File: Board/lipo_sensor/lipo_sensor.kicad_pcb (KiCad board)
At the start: 2 copper layers, 33 x 30.5 mm, 27 parts, among them IC1 ATMEGA328P-A, P1 CONN_02X03, P2 CONN_01X03, P3 CONN_01X07, P4 CONN_01X03, X1 CRYSTAL_SMD, Y1 Crystal

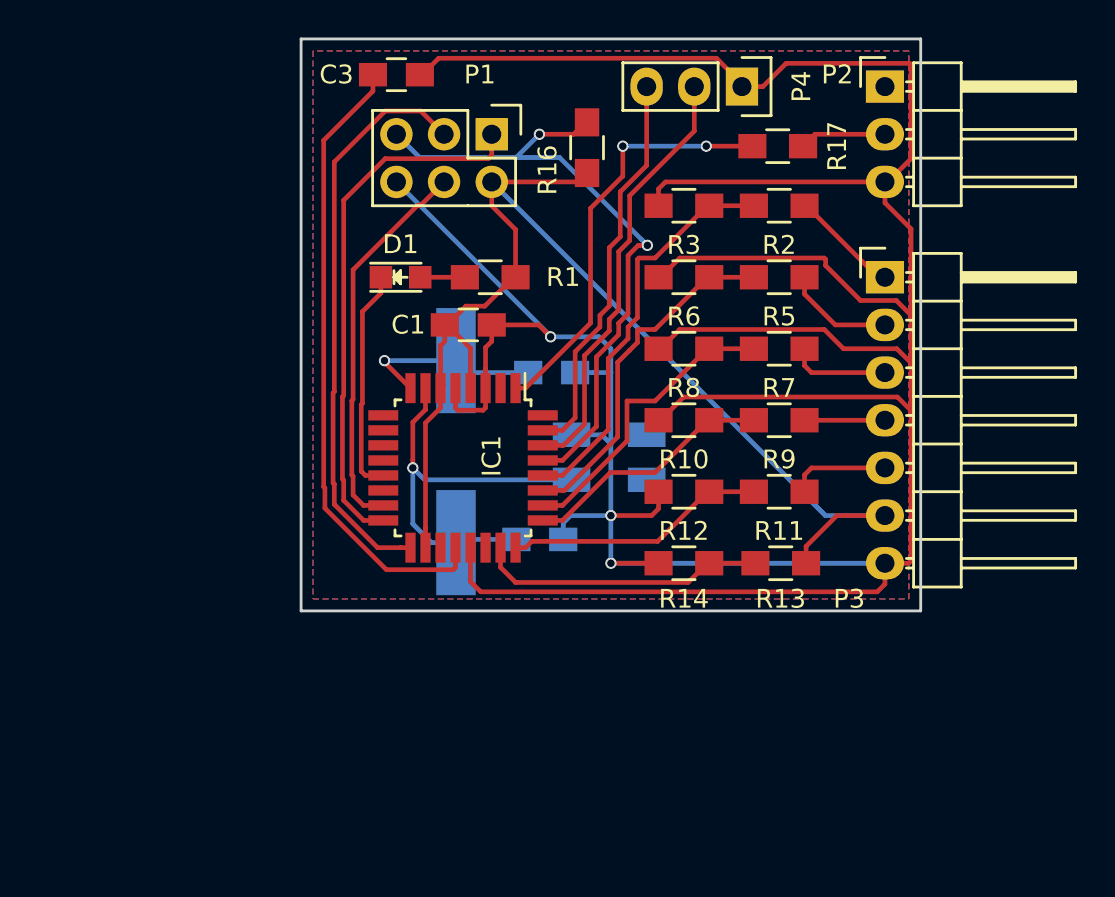
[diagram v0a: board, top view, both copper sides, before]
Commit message: Shrink layout and fix oszillator connections.
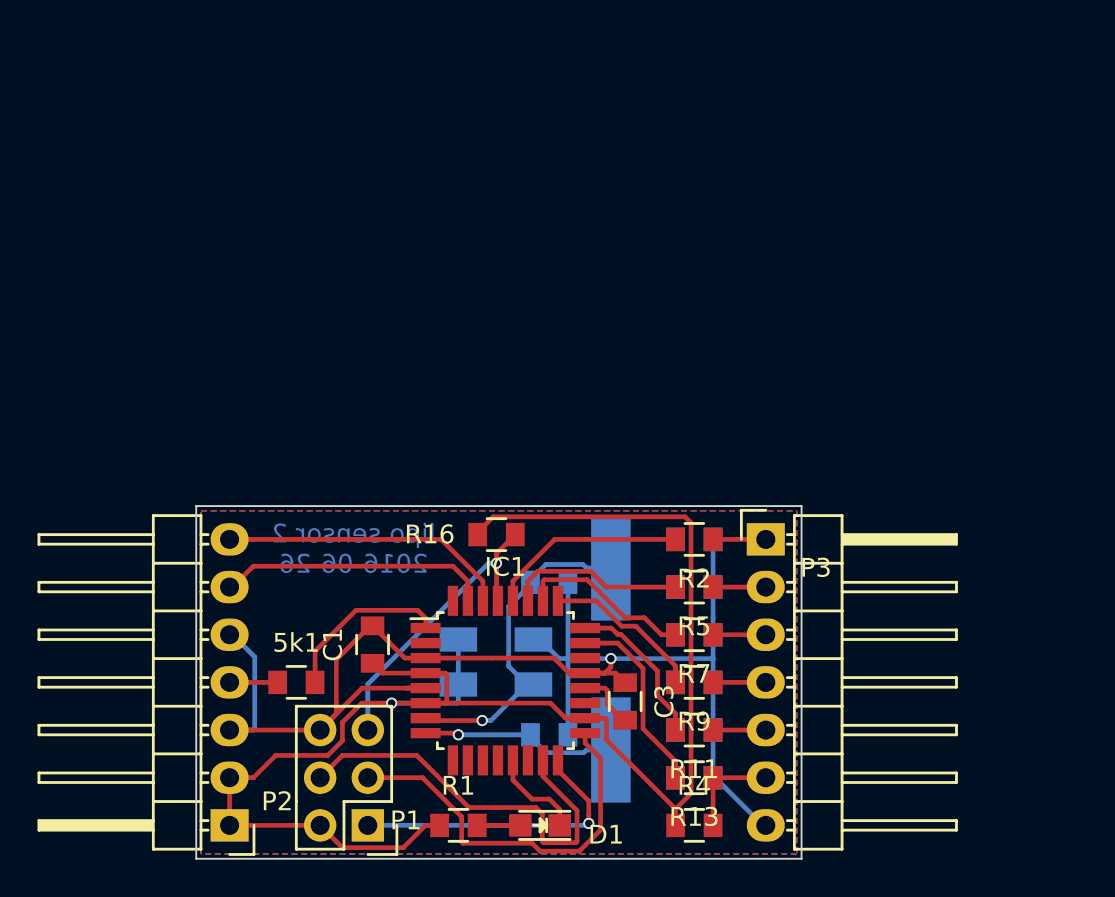
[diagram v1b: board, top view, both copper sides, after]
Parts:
- removed R17: 5k, Resistors_SMD:R_0805_HandSoldering
- removed X1: CRYSTAL_SMD, Crystals:Crystal_SMD_5032_4Pads
- added 5k1: 4k7, Capacitors_SMD:C_0805, F.Cu at (148.3, 110.5)
- added R4: 0, Capacitors_SMD:C_0805, F.Cu at (169.5, 118.1)
- C1, C3: footprint Capacitors_SMD:C_0805_HandSoldering -> Capacitors_SMD:C_0805
- C2, C5: value 16pF -> 22pF; footprint Capacitors_SMD:C_0805_HandSoldering -> Capacitors_SMD:C_0805
- P2: value CONN_01X03 -> CONN_01X07; footprint Pin_Headers:Pin_Header_Angled_1x03 -> Pin_Headers:Pin_Header_Angled_1x07
- P4: value CONN_01X03 -> OSZILLATOR; footprint Pin_Headers:Pin_Header_Straight_1x03 -> Cody_Footprints:Oszillator_SMD_5032_4Pads; moved to B.Cu
- R1: value 600 -> 680; footprint Resistors_SMD:R_0805_HandSoldering -> Capacitors_SMD:C_0805
- R10: value R -> 1k8; footprint Resistors_SMD:R_0805_HandSoldering -> Capacitors_SMD:C_0805; moved to B.Cu
- R11: value R -> 15k; footprint Resistors_SMD:R_0805_HandSoldering -> Capacitors_SMD:C_0805
- R12: value R -> 2k2; footprint Resistors_SMD:R_0805_HandSoldering -> Capacitors_SMD:C_0805; moved to B.Cu
- R13: value R -> 12k; footprint Resistors_SMD:R_0805_HandSoldering -> Capacitors_SMD:C_0805
- R14: value R -> 3k9; footprint Resistors_SMD:R_0805_HandSoldering -> Capacitors_SMD:C_0805; moved to B.Cu
- R16: footprint Resistors_SMD:R_0805_HandSoldering -> Capacitors_SMD:C_0805
- R2, R5, R9: value R -> 22k; footprint Resistors_SMD:R_0805_HandSoldering -> Capacitors_SMD:C_0805
- R3, R6: value R -> 1k; footprint Resistors_SMD:R_0805_HandSoldering -> Capacitors_SMD:C_0805; moved to B.Cu
- R7: value R -> 18k; footprint Resistors_SMD:R_0805_HandSoldering -> Capacitors_SMD:C_0805
- R8: value R -> 1k2; footprint Resistors_SMD:R_0805_HandSoldering -> Capacitors_SMD:C_0805; moved to B.Cu
- moved P2 52.6 mm to (144.8, 118.1), turned to 180 degrees
- moved P1 37.4 mm to (152.1, 118.1), turned to 180 degrees
- moved C3 35.6 mm to (165.9, 111.5), turned to 270 degrees
- moved P4 33.4 mm to (159.0, 109.4), turned to 0 degrees
- moved D1 30.1 mm to (161.3, 118.1), turned to 180 degrees
- moved R1 29.3 mm to (157.0, 118.1), turned to 0 degrees
- moved R16 21.2 mm to (159.0, 102.6), turned to 0 degrees
- moved C5 19.3 mm to (161.8, 113.3)
- moved R2 18.3 mm to (169.5, 102.9)
- moved R3 17.8 mm to (169.5, 102.9), turned to 0 degrees
- moved C1 17.8 mm to (152.4, 108.5), turned to 90 degrees
- moved R5 17.1 mm to (169.5, 105.4)
- moved R6 16.5 mm to (169.5, 105.4), turned to 0 degrees
- moved R7 15.9 mm to (169.5, 108.0)
- moved P3 15.3 mm to (173.4, 102.9)
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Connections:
- P2 pad 1: (no net) -> VCC
- P2 pad 2: Net-(P2-Pad2) -> VCC
- P3 pad 6: VCC -> Net-(P3-Pad6)
- P4 pad 1: GND -> VCC
- P4 pad 2: /RX -> GND
- P4 pad 3: /TX -> Net-(C2-Pad2)
- R13 pad 1: VCC -> Net-(P3-Pad6)
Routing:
- net GND: track 205.5 -> 77.6 mm, vias 3 -> 1
- net Net-(C3-Pad2): track 33.6 -> 3.28 mm
- net Net-(IC1-Pad29): track 35.1 -> 16.0 mm, vias 2 -> 1
- net VCC: track 68.9 -> 84.8 mm, vias 0 -> 1
- net /S.Port: track 22.5 -> 9.16 mm, vias 2 -> 0
- net Net-(IC1-Pad16): track 28.6 -> 15.9 mm, vias 0 -> 1
- net /Cell6: track 21.6 -> 10.6 mm
- net Net-(IC1-Pad17): track 30.8 -> 20.8 mm
- net /Cell5: track 18.6 -> 9.48 mm
- net /RX: track 23.6 -> 15.5 mm
- net /LED: track 12.0 -> 5.04 mm
- net /TX: track 21.2 -> 14.5 mm
- net /Cell4: track 16.0 -> 9.36 mm
- net /Cell2: track 13.9 -> 8.35 mm
- net Net-(P3-Pad6): track 0.00 -> 5.35 mm
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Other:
- board size 33 x 30.5 mm -> 32.3 x 18.8 mm
- net class Default: clearance 0.25 -> 0.2
- rule pad_to_mask_clearance: 0.2 -> 0
- rule trace_clearance: 0.25 -> 0.2
- board text added: "lipo sensor 2 2016-06-26"
- board text removed: "lipo sensor 1 2016-04-26"

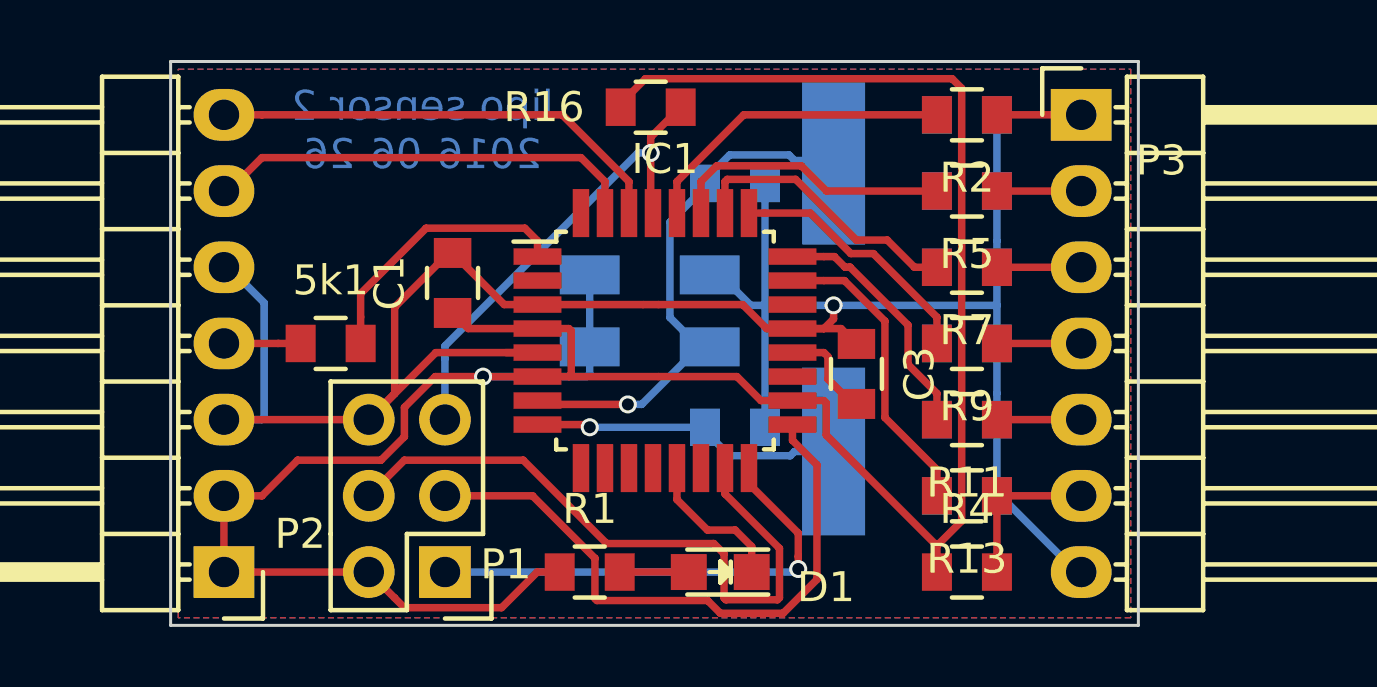
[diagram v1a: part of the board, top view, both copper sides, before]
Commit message: Fix inverted RX/TX.
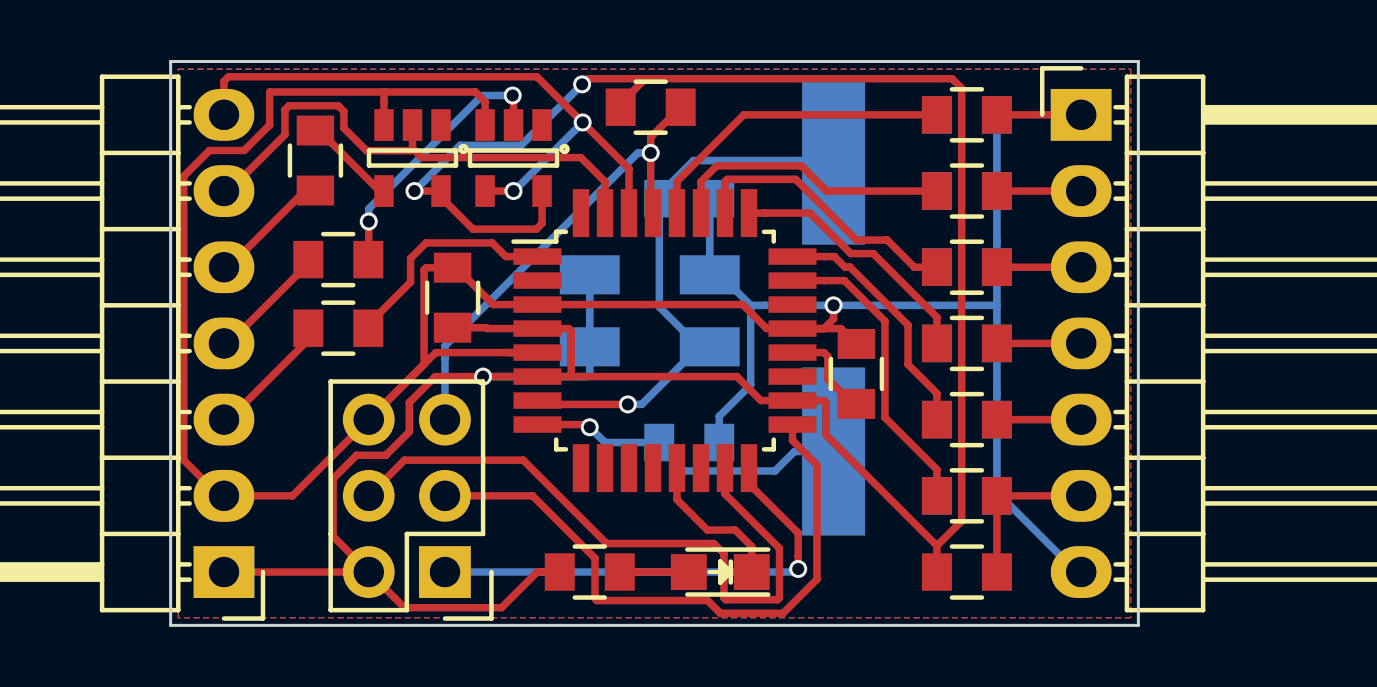
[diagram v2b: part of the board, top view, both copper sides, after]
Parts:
- added P5: INVERTER, TO_SOT_Packages_SMD:SOT-23-5, F.Cu at (151.1, 104.3)
- added P6: INVERTER, TO_SOT_Packages_SMD:SOT-23-5, F.Cu at (154.4, 104.3)
- added R15: R, Capacitors_SMD:C_0805, F.Cu at (147.8, 104.4)
- added R17: R, Capacitors_SMD:C_0805, F.Cu at (148.6, 107.7)
- moved C2 1.61 mm to (160.3, 105.7)
- moved C5 1.61 mm to (160.3, 113.8)
- moved 5k1 0.57 mm to (148.6, 110.0)
- moved C1 0.49 mm to (152.4, 109.0)
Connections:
- P2 pad 2: VCC -> GND
- P2 pad 3: GND -> Net-(5k1-Pad1)
- P2 pad 4: Net-(5k1-Pad1) -> Net-(P2-Pad4)
- P2 pad 5: GND -> Net-(P2-Pad5)
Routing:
- net GND: track 77.6 -> 96.1 mm
- net VCC: track 84.8 -> 97.0 mm, vias 1 -> 3
- net Net-(P6-Pad2): track 0.00 -> 9.06 mm, vias 0 -> 2
- net /RX: track 15.5 -> 21.6 mm, vias 0 -> 2
- net Net-(P2-Pad5): track 0.00 -> 4.53 mm
- net Net-(P2-Pad4): track 0.00 -> 4.05 mm
- net Net-(P5-Pad4): track 0.00 -> 3.12 mm
- net /TX: track 14.5 -> 17.6 mm
- net Net-(5k1-Pad1): track 2.56 -> 4.30 mm
- net /S.Port: track 9.16 -> 7.54 mm
- net Net-(C2-Pad2): track 17.8 -> 18.5 mm

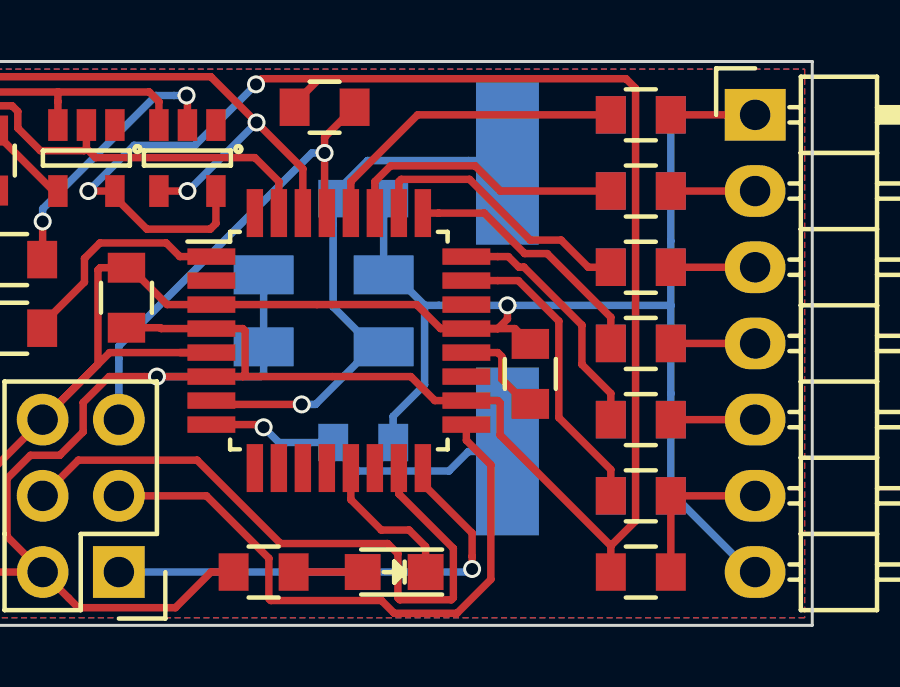
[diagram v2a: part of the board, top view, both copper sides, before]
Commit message: Replace big crystal with smaller crystal: QC5A Series 3.2x5.0 4-Pad SMD Quartz Crystal Unit
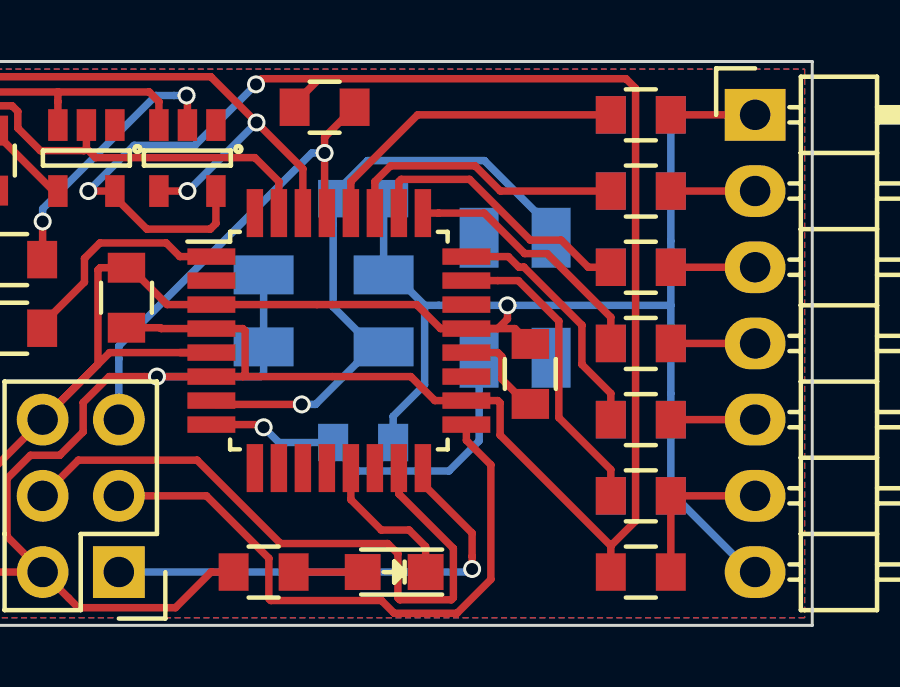
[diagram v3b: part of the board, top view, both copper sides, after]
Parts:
- removed Y1: Crystal, Crystals:Crystal_HC49-SD_SMD
- added P7: QUARZ, Cody_Footprints:Oszillator_SMD_5032_4Pads, B.Cu at (165.4, 109.0)
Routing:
- net Net-(C2-Pad2): track 18.5 -> 21.2 mm
- net Net-(C5-Pad2): track 10.9 -> 12.8 mm
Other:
- board text added: "lipo sensor 2 2016-06-28"
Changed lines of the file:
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@@
     (thickness 1.6)
     (drawings 6)
-    (tracks 286)
+    (tracks 287)
     (zones 0)
     (modules 31)
@@
   (layers
     (0 F.Cu signal hide)
-    (31 B.Cu signal hide)
+    (31 B.Cu signal)
     (32 B.Adhes user hide)
     (33 F.Adhes user hide)
@@
     )
   )
-  (module Crystals:Crystal_HC49-SD_SMD (layer B.Cu)
-    (at 165.1 109.24286 270)
-    (descr "Crystal Quarz HC49-SD SMD")
-    (tags "Crystal Quarz HC49-SD SMD")
-    (attr smd)
-    (fp_text reference Y1 (at 0 5.08 270) (layer B.SilkS) hide
-      (effects (font (size 1 1) (thickness 0.15)) (justify mirror))
-    )
-    (fp_text value Crystal (at 2.54 -5.08 270) (layer B.Fab)
-      (effects (font (size 1 1) (thickness 0.15)) (justify mirror))
-    )
-    (fp_circle (center 0 0) (end 0.8509 0) (layer B.Adhes) (width 0.381))
-    (fp_circle (center 0 0) (end 0.50038 0) (layer B.Adhes) (width 0.381))
-    (fp_circle (center 0 0) (end 0.14986 -0.0508) (layer B.Adhes) (width 0.381))
-    (fp_line (start -5.84962 -2.49936) (end 5.84962 -2.49936) (layer B.SilkS) (width 0.15))
-    (fp_line (start 5.84962 2.49936) (end -5.84962 2.49936) (layer B.SilkS) (width 0.15))
-    (fp_line (start 5.84962 -2.49936) (end 5.84962 -1.651) (layer B.SilkS) (width 0.15))
-    (fp_line (start 5.84962 2.49936) (end 5.84962 1.651) (layer B.SilkS) (width 0.15))
-    (fp_line (start -5.84962 -2.49936) (end -5.84962 -1.651) (layer B.SilkS) (width 0.15))
-    (fp_line (start -5.84962 2.49936) (end -5.84962 1.651) (layer B.SilkS) (width 0.15))
-    (pad 1 smd rect (at -4.84886 0 270) (size 5.6007 2.10058) (layers B.Cu B.Paste B.Mask)
-      (net 5 "Net-(C2-Pad2)"))
-    (pad 2 smd rect (at 4.84886 0 270) (size 5.6007 2.10058) (layers B.Cu B.Paste B.Mask)
-      (net 7 "Net-(C5-Pad2)"))
-  )
   (module Pin_Headers:Pin_Header_Angled_1x07 (layer F.Cu)
     (at 144.78 118.11 180)
@@
     )
   )
-  (gr_text "lipo sensor 2\n2016-06-26" (at 151.384 103.378) (layer B.SilkS)
+  (module Cody_Footprints:Oszillator_SMD_5032_4Pads (layer B.Cu)
+    (at 165.354 108.966 270)
+    (descr "Ceramic SMD crystal, 5.0x3.2mm, 4 Pads")
+    (tags "crystal oscillator quartz SMD SMT 5032")
+    (attr smd)
+    (fp_text reference P7 (at 0 3 270) (layer B.SilkS) hide
+      (effects (font (size 1 1) (thickness 0.15)) (justify mirror))
+    )
+    (fp_text value QUARZ (at 0 -3.25 270) (layer B.Fab)
+      (effects (font (size 1 1) (thickness 0.15)) (justify mirror))
+    )
+    (fp_line (start -2.6 -0.2) (end -3.3 -0.2) (layer B.SilkS) (width 0.15))
+    (fp_line (start -0.7 -1.7) (end -0.7 -2.2) (layer B.SilkS) (width 0.15))
+    (fp_line (start 2.5 -1.6) (end 2.5 1.6) (layer B.Fab) (width 0.15))
+    (fp_line (start -2.5 -1.6) (end 2.5 -1.6) (layer B.Fab) (width 0.15))
+    (fp_line (start -2.5 1.6) (end -2.5 -1.6) (layer B.Fab) (width 0.15))
+    (fp_line (start 2.5 1.6) (end -2.5 1.6) (layer B.Fab) (width 0.15))
+    (fp_line (start 3.5 -2.35) (end 3.5 2.35) (layer B.CrtYd) (width 0.05))
+    (fp_line (start -3.5 -2.35) (end 3.5 -2.35) (layer B.CrtYd) (width 0.05))
+    (fp_line (start -3.5 2.35) (end -3.5 -2.35) (layer B.CrtYd) (width 0.05))
+    (fp_line (start 3.5 2.35) (end -3.5 2.35) (layer B.CrtYd) (width 0.05))
+    (fp_line (start 0.70208 -1.7) (end -0.7 -1.7) (layer B.SilkS) (width 0.15))
+    (fp_line (start -0.70104 1.7) (end 0.70104 1.7) (layer B.SilkS) (width 0.15))
+    (fp_line (start 2.6 -0.2) (end 2.6 0.2) (layer B.SilkS) (width 0.15))
+    (fp_line (start -2.6 -0.2) (end -2.6 0.2) (layer B.SilkS) (width 0.15))
+    (pad 1 smd rect (at -2 -1.2 270) (size 2 1.3) (layers B.Cu B.Paste B.Mask)
+      (net 5 "Net-(C2-Pad2)"))
+    (pad 2 smd rect (at 2 -1.2 270) (size 2 1.3) (layers B.Cu B.Paste B.Mask))
+    (pad 3 smd rect (at 2 1.2 270) (size 2 1.3) (layers B.Cu B.Paste B.Mask)
+      (net 7 "Net-(C5-Pad2)"))
+    (pad 4 smd rect (at -2 1.2 270) (size 2 1.3) (layers B.Cu B.Paste B.Mask))
+    (model Crystals.3dshapes/Crystal_SMD_5032_4Pads.wrl
+      (at (xyz 0 0 0))
+      (scale (xyz 1 1 1))
+      (rotate (xyz 0 0 0))
+    )
+  )
+  (gr_text "lipo sensor 2\n2016-06-28" (at 151.384 103.378) (layer B.SilkS)
     (effects (font (size 1 1) (thickness 0.2)) (justify mirror))
   )
@@
   (segment (start 149.606 113.03) (end 151.840897 110.795103) (width 0.25) (layer F.Cu) (net 4))
   (segment (start 151.840897 110.795103) (end 155.229897 110.795103) (width 0.25) (layer F.Cu) (net 4))
+  (segment (start 160.435 104.394) (end 164.332 104.394) (width 0.25) (layer B.Cu) (net 5))
+  (segment (start 164.332 104.394) (end 166.554 106.616) (width 0.25) (layer B.Cu) (net 5))
+  (segment (start 166.554 106.616) (end 166.554 106.966) (width 0.25) (layer B.Cu) (net 5))
   (segment (start 159.29 105.664) (end 159.29 105.539) (width 0.25) (layer B.Cu) (net 5))
   (segment (start 159.29 105.539) (end 160.435 104.394) (width 0.25) (layer B.Cu) (net 5))
-  (segment (start 160.435 104.394) (end 163.79971 104.394) (width 0.25) (layer B.Cu) (net 5))
-  (segment (start 163.79971 104.394) (end 165.1 104.394) (width 0.25) (layer B.Cu) (net 5))
   (segment (start 160.972 110.604) (end 160.622 110.604) (width 0.25) (layer B.Cu) (net 5))
   (segment (start 160.622 110.604) (end 159.29 109.272) (width 0.25) (layer B.Cu) (net 5))
@@
   (segment (start 164.911999 110.927205) (end 164.779897 110.795103) (width 0.25) (layer F.Cu) (net 6))
   (segment (start 164.779897 110.795103) (end 163.729897 110.795103) (width 0.25) (layer F.Cu) (net 6))
+  (segment (start 159.29 113.792) (end 159.29 113.917) (width 0.25) (layer B.Cu) (net 7))
+  (segment (start 159.29 113.917) (end 160.115001 114.742001) (width 0.25) (layer B.Cu) (net 7))
+  (segment (start 160.115001 114.742001) (end 163.149429 114.742001) (width 0.25) (layer B.Cu) (net 7))
+  (segment (start 163.149429 114.742001) (end 164.154 113.73743) (width 0.25) (layer B.Cu) (net 7))
+  (segment (start 164.154 113.73743) (end 164.154 110.966) (width 0.25) (layer B.Cu) (net 7))
   (segment (start 159.29 113.792) (end 157.48 113.792) (width 0.25) (layer B.Cu) (net 7))
   (segment (start 157.48 113.792) (end 156.972 113.284) (width 0.25) (layer B.Cu) (net 7))
-  (segment (start 165.1 114.09172) (end 163.79971 114.09172) (width 0.25) (layer B.Cu) (net 7))
-  (segment (start 163.79971 114.09172) (end 163.149429 114.742001) (width 0.25) (layer B.Cu) (net 7))
-  (segment (start 160.115001 114.742001) (end 159.29 113.917) (width 0.25) (layer B.Cu) (net 7))
-  (segment (start 163.149429 114.742001) (end 160.115001 114.742001) (width 0.25) (layer B.Cu) (net 7))
-  (segment (start 159.29 113.917) (end 159.29 113.792) (width 0.25) (layer B.Cu) (net 7))
   (segment (start 155.229897 113.195103) (end 156.883103 113.195103) (width 0.25) (layer F.Cu) (net 7))
   (segment (start 156.883103 113.195103) (end 156.972 113.284) (width 0.25) (layer F.Cu) (net 7))
